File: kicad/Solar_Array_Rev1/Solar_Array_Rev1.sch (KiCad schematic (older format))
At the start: 36 parts, among them IC1 TVS_4x4, IC2 SPV1040, IC3 LTC2990.1, IC4 TVS_4x4, P1 PV_IN, P2 CONN_01X07, Q1 Q_NMOS_DGS, Q2 Q_PMOS_DGS, Q3 Q_NPN_BCE

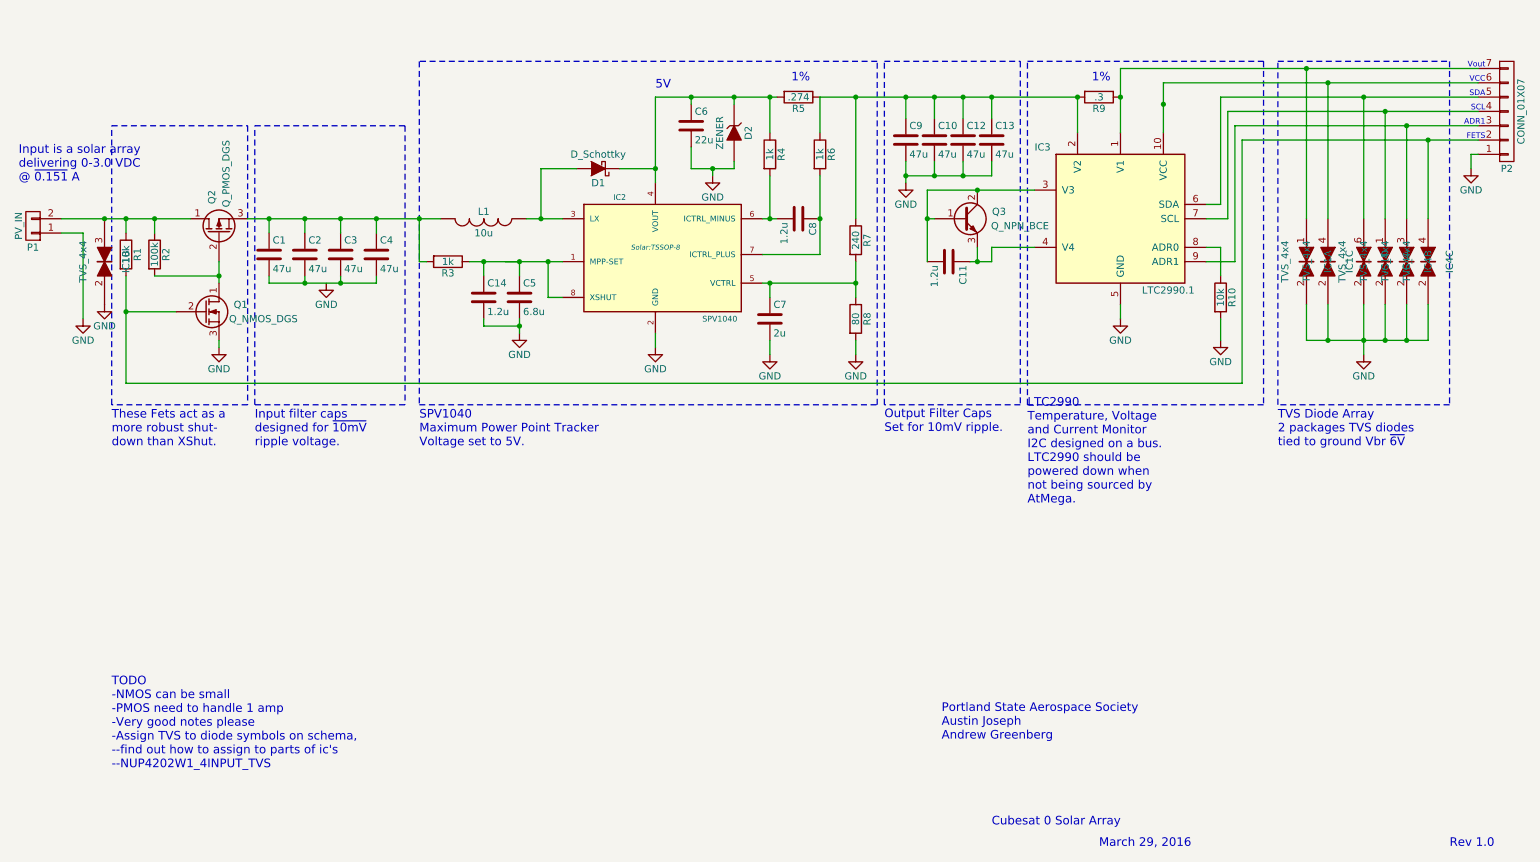
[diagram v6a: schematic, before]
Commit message: Removed old files, repaired broken schema, finished layout.
-Removed old SVG DRL and  GBR files
-Removed old PDF files
-Fixed broken TVS_4x4 Schematic and updated footprint
-PCB file created
-Board layout finished
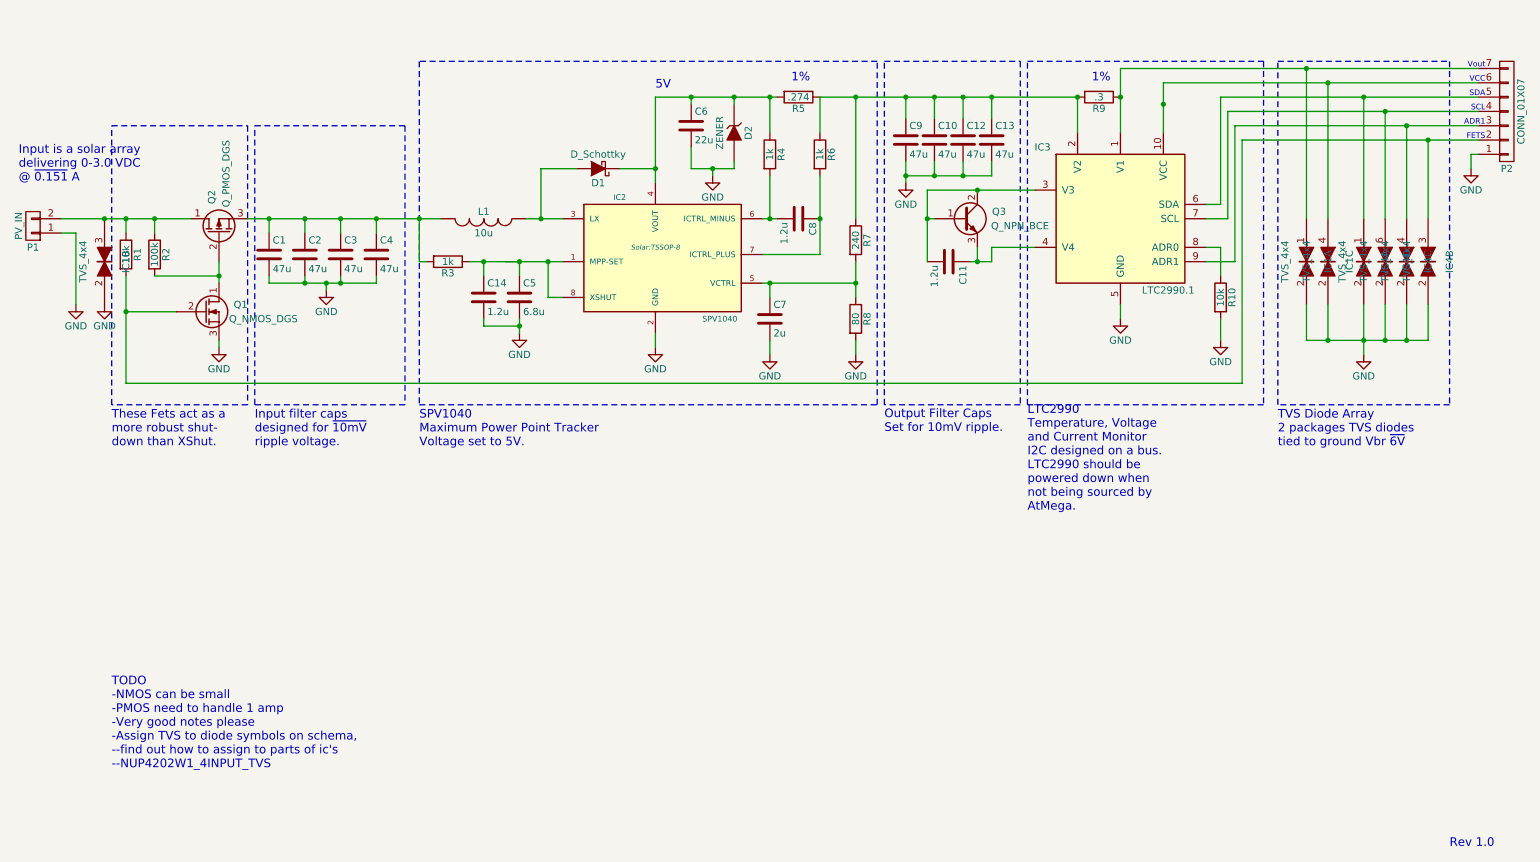
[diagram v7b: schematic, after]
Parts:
- C11, C14, C8: footprint Capacitors_SMD:C_0603 -> Capacitors_SMD:C_0805
- Q1: footprint TO_SOT_Packages_SMD:SOT-223 -> TO_SOT_Packages_SMD:SC-70
- renumbered IC1 to IC4
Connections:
- net GND: now also C1.2, C2.2, C3.2, C4.2
- net at P2.2 (P2), Q1.2 (G), R1.2: now also IC4.3; no longer IC4.4
- net at IC3.9 (ADR1), P2.3 (P3): now also IC4.4; no longer IC4.3
- net at IC3.7 (SCL), P2.4 (P4): now also IC4.6; no longer IC4.1
- net at IC3.6 (SDA), P2.5 (P5): now also IC4.1; no longer IC4.6
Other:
- note removed: "Cubesat 0 Solar Array"
- note removed: "March 29, 2016"
- note removed: "Portland State Aerospace Society\nAustin Joseph\nAndrew Greenberg"
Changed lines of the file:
@@
 encoding utf-8
 Sheet 1 1
-Title ""
-Date ""
-Rev ""
-Comp ""
-Comment1 ""
-Comment2 ""
+Title "Cubesat Power System"
+Date "2016-03-29"
+Rev "Rev 1"
+Comp "Portland State Aerospace Society"
+Comment1 "Austin Joseph"
+Comment2 "Andrew Greenberg"
 Comment3 ""
 Comment4 ""
@@
 $EndComp
 $Comp
-L GND #PWR4
+L GND #PWR01
 U 1 1 56FC2522
-P 2750 3700
-F 0 "#PWR4" H 2750 3450 50  0001 C CNN
-F 1 "GND" H 2750 3550 50  0000 C CNN
-F 2 "" H 2750 3700 50  0000 C CNN
-F 3 "" H 2750 3700 50  0000 C CNN
-	1    2750 3700
-	1    0    0    -1
-$EndComp
-$Comp
-L GND #PWR6
+P 2750 3750
+F 0 "#PWR01" H 2750 3500 50  0001 C CNN
+F 1 "GND" H 2750 3600 50  0000 C CNN
+F 2 "" H 2750 3750 50  0000 C CNN
+F 3 "" H 2750 3750 50  0000 C CNN
+	1    2750 3750
+	1    0    0    -1
+$EndComp
+$Comp
+L GND #PWR02
 U 1 1 56FC25A8
 P 5050 4150
-F 0 "#PWR6" H 5050 3900 50  0001 C CNN
+F 0 "#PWR02" H 5050 3900 50  0001 C CNN
 F 1 "GND" H 5050 4000 50  0000 C CNN
 F 2 "" H 5050 4150 50  0000 C CNN
@@
 $EndComp
 $Comp
-L GND #PWR5
+L GND #PWR03
 U 1 1 56FC26B3
 P 4100 4050
-F 0 "#PWR5" H 4100 3800 50  0001 C CNN
+F 0 "#PWR03" H 4100 3800 50  0001 C CNN
 F 1 "GND" H 4100 3900 50  0000 C CNN
 F 2 "" H 4100 4050 50  0000 C CNN
@@
 F 0 "C8" H 6075 3350 50  0000 L CNN
 F 1 "1.2u" H 6075 3150 50  0000 L CNN
-F 2 "Capacitors_SMD:C_0603" H 6088 3100 50  0001 C CNN
+F 2 "Capacitors_SMD:C_0805" H 6088 3100 50  0001 C CNN
 F 3 "" H 6050 3250 50  0000 C CNN
 	1    6050 3250
@@
 $EndComp
 $Comp
-L GND #PWR7
+L GND #PWR04
 U 1 1 56FC2C93
 P 5450 2950
-F 0 "#PWR7" H 5450 2700 50  0001 C CNN
+F 0 "#PWR04" H 5450 2700 50  0001 C CNN
 F 1 "GND" H 5450 2800 50  0000 C CNN
 F 2 "" H 5450 2950 50  0000 C CNN
@@
 $EndComp
 $Comp
-L GND #PWR9
+L GND #PWR05
 U 1 1 56FC2E7A
 P 6450 4200
-F 0 "#PWR9" H 6450 3950 50  0001 C CNN
+F 0 "#PWR05" H 6450 3950 50  0001 C CNN
 F 1 "GND" H 6450 4050 50  0000 C CNN
 F 2 "" H 6450 4200 50  0000 C CNN
@@
 $EndComp
 $Comp
-L GND #PWR10
+L GND #PWR06
 U 1 1 56FC34A1
 P 6800 3000
-F 0 "#PWR10" H 6800 2750 50  0001 C CNN
+F 0 "#PWR06" H 6800 2750 50  0001 C CNN
 F 1 "GND" H 6800 2850 50  0000 C CNN
 F 2 "" H 6800 3000 50  0000 C CNN
@@
 $EndComp
 Connection ~ 2600 3250
-Wire Wire Line
-	900  3350 1050 3350
-Wire Wire Line
-	1050 3350 1050 3950
-$Comp
-L GND #PWR1
+$Comp
+L GND #PWR07
 U 1 1 56FC3723
-P 1050 3950
-F 0 "#PWR1" H 1050 3700 50  0001 C CNN
-F 1 "GND" H 1050 3800 50  0000 C CNN
-F 2 "" H 1050 3950 50  0000 C CNN
-F 3 "" H 1050 3950 50  0000 C CNN
-	1    1050 3950
+P 1000 3850
+F 0 "#PWR07" H 1000 3600 50  0001 C CNN
+F 1 "GND" H 1000 3700 50  0000 C CNN
+F 2 "" H 1000 3850 50  0000 C CNN
+F 3 "" H 1000 3850 50  0000 C CNN
+	1    1000 3850
 	1    0    0    -1
 $EndComp
@@
 F 0 "C11" H 7125 3650 50  0000 L CNN
 F 1 "1.2u" H 7125 3450 50  0000 L CNN
-F 2 "Capacitors_SMD:C_0603" H 7138 3400 50  0001 C CNN
+F 2 "Capacitors_SMD:C_0805" H 7138 3400 50  0001 C CNN
 F 3 "" H 7100 3550 50  0000 C CNN
 	1    7100 3550
@@
 	9050 2500 9050 3250
 $Comp
-L GND #PWR11
+L GND #PWR08
 U 1 1 56FCAF6F
 P 8300 3950
-F 0 "#PWR11" H 8300 3700 50  0001 C CNN
+F 0 "#PWR08" H 8300 3700 50  0001 C CNN
 F 1 "GND" H 8300 3800 50  0000 C CNN
 F 2 "" H 8300 3950 50  0000 C CNN
@@
 	8900 3450 9000 3450
 $Comp
-L GND #PWR12
+L GND #PWR09
 U 1 1 56FCBA35
 P 9000 4100
-F 0 "#PWR12" H 9000 3850 50  0001 C CNN
+F 0 "#PWR09" H 9000 3850 50  0001 C CNN
 F 1 "GND" H 9000 3950 50  0000 C CNN
 F 2 "" H 9000 4100 50  0000 C CNN
@@
 	9150 2700 10800 2700
 $Comp
-L GND #PWR14
+L GND #PWR010
 U 1 1 56FCEB98
 P 10750 2900
-F 0 "#PWR14" H 10750 2650 50  0001 C CNN
+F 0 "#PWR010" H 10750 2650 50  0001 C CNN
 F 1 "GND" H 10750 2750 50  0000 C CNN
 F 2 "" H 10750 2900 50  0000 C CNN
@@
 $EndComp
 $Comp
-L GND #PWR8
+L GND #PWR011
 U 1 1 56FD0196
 P 5850 4200
-F 0 "#PWR8" H 5850 3950 50  0001 C CNN
+F 0 "#PWR011" H 5850 3950 50  0001 C CNN
 F 1 "GND" H 5850 4050 50  0000 C CNN
 F 2 "" H 5850 4200 50  0000 C CNN
@@
 	6450 4100 6450 4200
 $Comp
-L GND #PWR2
+L GND #PWR012
 U 1 1 56FC80D2
 P 1200 3850
-F 0 "#PWR2" H 1200 3600 50  0001 C CNN
+F 0 "#PWR012" H 1200 3600 50  0001 C CNN
 F 1 "GND" H 1200 3700 50  0000 C CNN
 F 2 "" H 1200 3850 50  0000 C CNN
@@
 Text Notes 10850 2600 2    39   ~ 0
 ADR1
-Text Notes 7400 7500 0    60   ~ 0
-Cubesat 0 Solar Array
 Text Notes 10600 7650 0    60   ~ 0
 Rev 1.0
-Text Notes 8150 7650 0    60   ~ 0
-March 29, 2016
-Text Notes 7050 6900 0    60   ~ 0
-Portland State Aerospace Society\nAustin Joseph\nAndrew Greenberg
 Text Notes 10850 2500 2    39   ~ 0
 SCL
@@
 F 0 "Q1" H 2200 3950 50  0000 R CNN
 F 1 "Q_NMOS_DGS" H 2550 3850 50  0000 R CNN
-F 2 "TO_SOT_Packages_SMD:SOT-223" H 2100 4000 50  0001 C CNN
+F 2 "TO_SOT_Packages_SMD:SC-70" H 2100 4000 50  0001 C CNN
 F 3 "" H 1900 3900 50  0000 C CNN
 	1    1900 3900
@@
 	2000 4100 2000 4150
 $Comp
-L GND #PWR3
+L GND #PWR013
 U 1 1 5709901A
 P 2000 4150
-F 0 "#PWR3" H 2000 3900 50  0001 C CNN
+F 0 "#PWR013" H 2000 3900 50  0001 C CNN
 F 1 "GND" H 2000 4000 50  0000 C CNN
 F 2 "" H 2000 4150 50  0000 C CNN
@@
 Connection ~ 9750 4100
 $Comp
-L GND #PWR13
+L GND #PWR014
 U 1 1 570C3955
 P 10000 4200
-F 0 "#PWR13" H 10000 3950 50  0001 C CNN
+F 0 "#PWR014" H 10000 3950 50  0001 C CNN
 F 1 "GND" H 10000 4050 50  0000 C CNN
 F 2 "" H 10000 4200 50  0000 C CNN
@@
 $EndComp
 $Comp
-L TVS_4x4 IC1
-U 4 1 570C29BF
+L TVS_4x4 IC4
+U 1 1 570C29BF
 P 10000 3550
-F 0 "IC1" H 10000 3700 50  0000 C CNN
+F 0 "IC4" H 10000 3700 50  0000 C CNN
 F 1 "TVS_4x4" H 10000 3400 50  0000 C CNN
 F 2 "TO_SOT_Packages_SMD:SC-70-6" H 10000 3550 50  0001 C CNN
 F 3 "" H 10000 3550 50  0000 C CNN
-	4    10000 3550
+	1    10000 3550
 	0    1    1    0
 $EndComp
 $Comp
 L TVS_4x4 IC4
-U 1 1 570C2A53
+U 4 1 570C2A53
 P 10150 3550
 F 0 "IC4" H 10150 3700 50  0000 C CNN
@@
 F 2 "TO_SOT_Packages_SMD:SC-70-6" H 10150 3550 50  0001 C CNN
 F 3 "" H 10150 3550 50  0000 C CNN
-	1    10150 3550
+	4    10150 3550
 	0    1    1    0
 $EndComp
 $Comp
 L TVS_4x4 IC4
-U 2 1 570C2BB5
+U 3 1 570C2BB5
 P 10300 3550
 F 0 "IC4" H 10300 3700 50  0000 C CNN
@@
 F 2 "TO_SOT_Packages_SMD:SC-70-6" H 10300 3550 50  0001 C CNN
 F 3 "" H 10300 3550 50  0000 C CNN
-	2    10300 3550
+	3    10300 3550
 	0    1    1    0
 $EndComp
 $Comp
 L TVS_4x4 IC4
-U 3 1 570C2C73
+U 2 1 570C2C73
 P 10450 3550
 F 0 "IC4" H 10450 3700 50  0000 C CNN
@@
 F 2 "TO_SOT_Packages_SMD:SC-70-6" H 10450 3550 50  0001 C CNN
 F 3 "" H 10450 3550 50  0000 C CNN
-	3    10450 3550
+	2    10450 3550
 	0    1    1    0
 $EndComp
@@
 Text Notes 6650 4750 0    60   ~ 0
 Output Filter Caps\nSet for 10mV ripple.
-Text Notes 7650 5250 0    60   ~ 0
+Text Notes 7650 5300 0    60   ~ 0
 LTC2990\nTemperature, Voltage\nand Current Monitor\nI2C designed on a bus.\nLTC2990 should be\npowered down when\nnot being sourced by\nAtMega.
 Text Notes 9400 4850 0    60   ~ 0
@@
 F 0 "C14" H 3875 3900 50  0000 L CNN
 F 1 "1.2u" H 3875 3700 50  0000 L CNN
-F 2 "Capacitors_SMD:C_0603" H 3888 3650 50  0001 C CNN
+F 2 "Capacitors_SMD:C_0805" H 3888 3650 50  0001 C CNN
 F 3 "" H 3850 3800 50  0000 C CNN
 	1    3850 3800
@@
 	3850 4000 4100 4000
 Connection ~ 4100 4000
+Wire Wire Line
+	900  3350 1000 3350
+Wire Wire Line
+	1000 3350 1000 3850
+Wire Wire Line
+	2750 3750 2750 3700
+Connection ~ 2750 3700
 $EndSCHEMATC

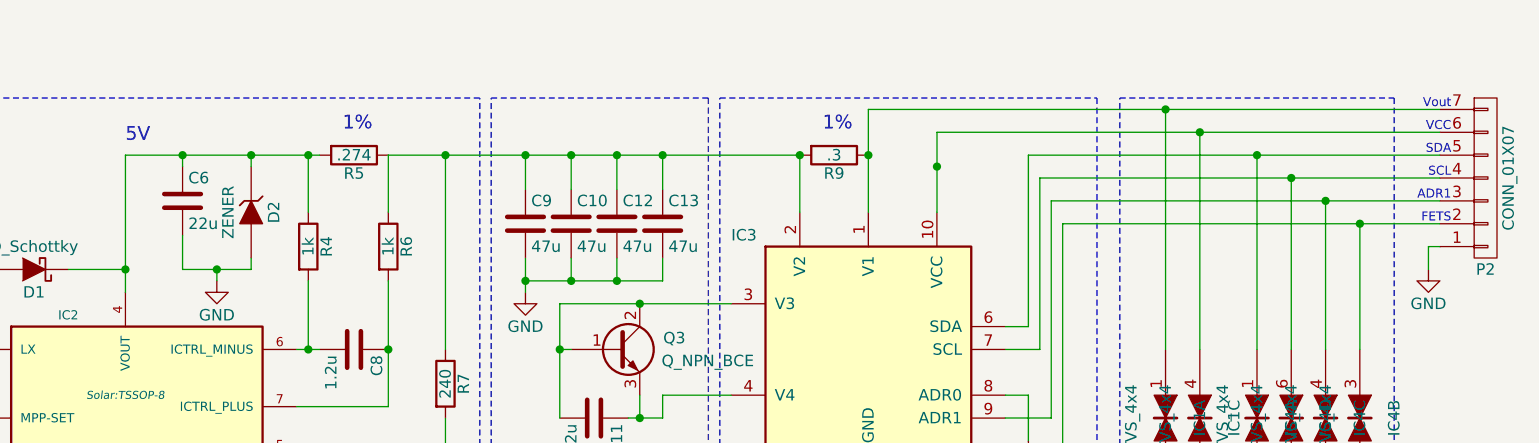
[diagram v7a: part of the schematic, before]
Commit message: Removed D2.  Set R9 as NP resistor and tied sensor to R5.
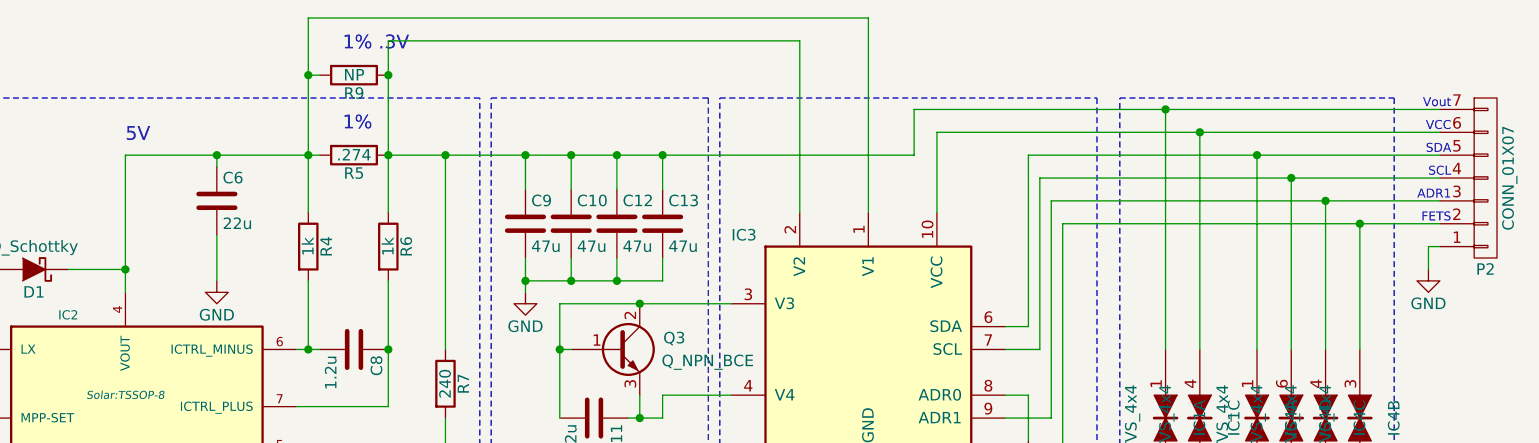
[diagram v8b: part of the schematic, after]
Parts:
- removed D2: ZENER, Diodes_SMD:SOD-323, symbol ZENER
- R9: value .3 -> NP
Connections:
- net at C6.1, D1.1 (K), IC2.4 (VOUT)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: now also IC3.1 (V1), R9.2
- net at C10.1, C12.1, C13.1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: now also IC1.1, P2.7 (P7), R9.1; no longer R9.2
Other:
- note added: "1% .3V"
- moved on the sheet: C6, R9
